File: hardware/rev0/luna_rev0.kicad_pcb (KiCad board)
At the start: 4 copper layers, 48 x 48 mm, 202 parts, among them IC1 ECP5-BGA256, J1 USB_C_Receptacle_USB2.0, J10 TC_SWD, J11 PMOD_B, J2 USB_C_Receptacle_USB2.0, J3 USB_A, J4 USB_C_Receptacle_USB2.0, J5 Conn_FPGA_JTAG_10, J6 Conn_ARM_JTAG_SWD_10, J7 PMOD_A, J8 Conn_Coaxial, J9 Conn_Coaxial, SW1 BTN_DFU, SW2 BTN_RESET, U1 AP22811A, U10 HyperRAM, U11 USB3343, U12 AP22811A, U13 AP22811A, U14 74AUP2G126, U2 74AUP2G126, U3 AP7366-33W5-7, U4 TCR2EF115, U5 MIC5504-2.5YM5, U6 ATSAMD11D14A-MUT, U7 W25Q32JVSS, U8 USB3343, U9 USB3343, Y1 Osc60MHz

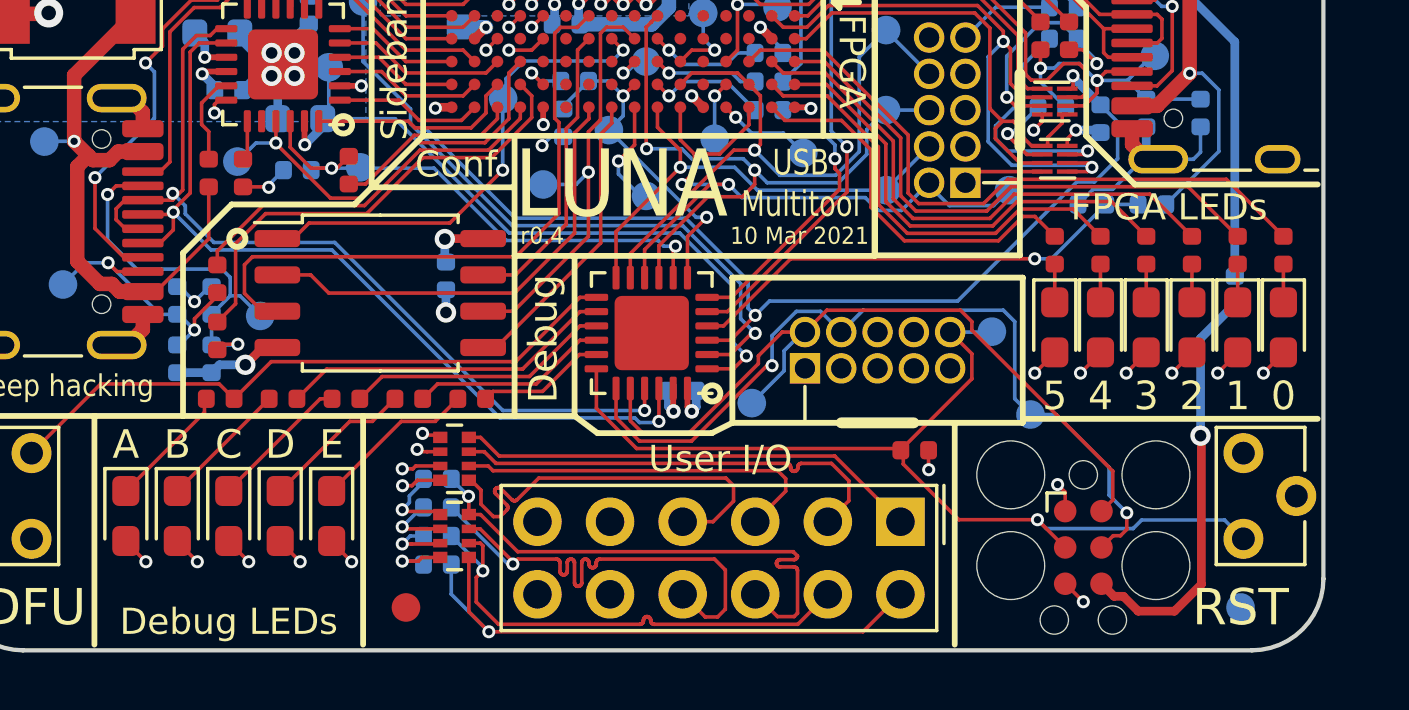
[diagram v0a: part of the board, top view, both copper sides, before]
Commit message: U6 moved, silk aligned, J6/+3V3 connected
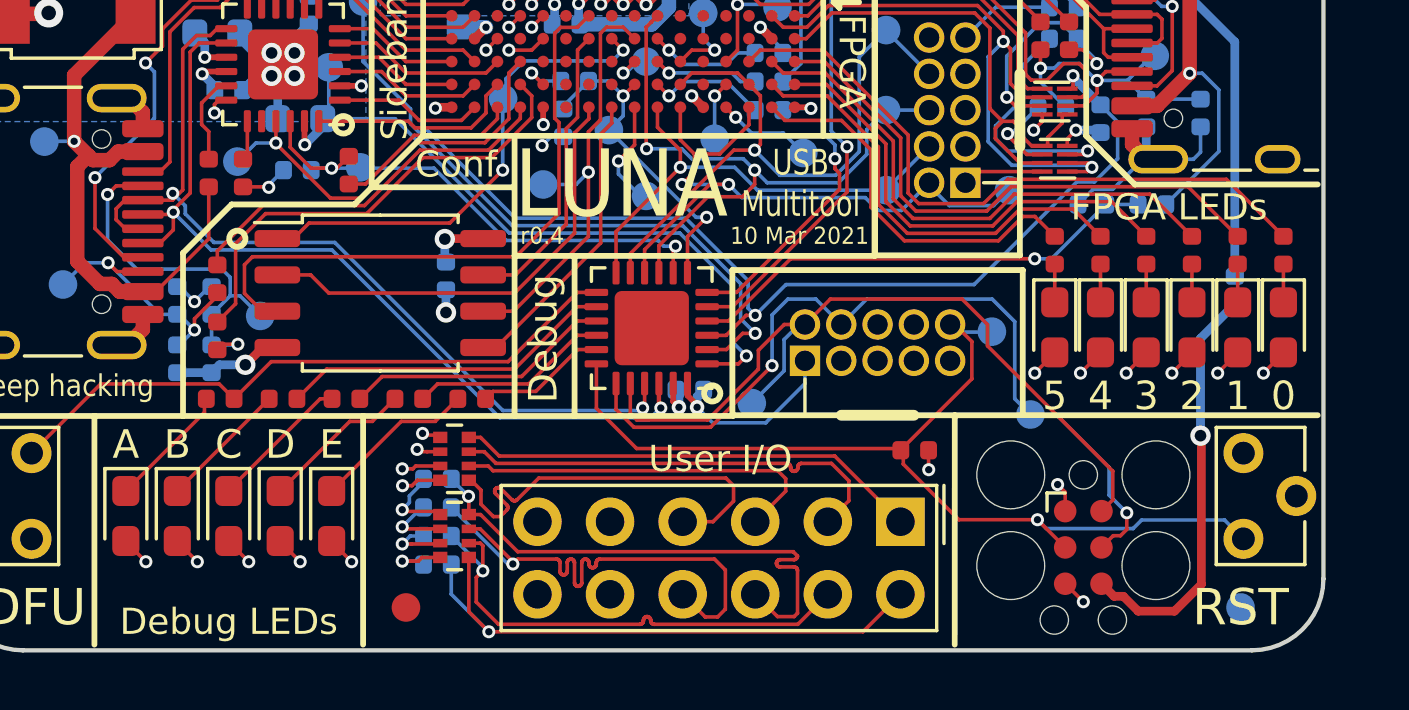
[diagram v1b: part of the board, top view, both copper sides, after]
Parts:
- moved J6 0.27 mm to (122.9, 102.2)
- moved C14 0.26 mm to (116.3, 103.9)
- moved U6 0.17 mm to (115.0, 101.7)
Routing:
- net +3V3: track 80.1 -> 85.5 mm
- net /FPGA Configuration and Dev Features/UC_SWDCLK: track 29.2 -> 29.8 mm
- net /FPGA Configuration and Dev Features/UC_SWDIO: track 27.5 -> 28.0 mm
